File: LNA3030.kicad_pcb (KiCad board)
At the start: 4 copper layers, 11.7 x 8.7 mm, 25 parts, among them P1 SMA-KIT-1.5MF, U1 SWITCH, U2 SWITCH, U3 LNA, U4 SAW

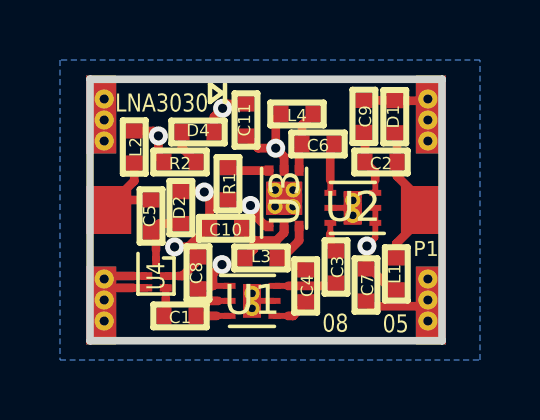
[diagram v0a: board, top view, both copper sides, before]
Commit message: modify for DCC6C SAW filters
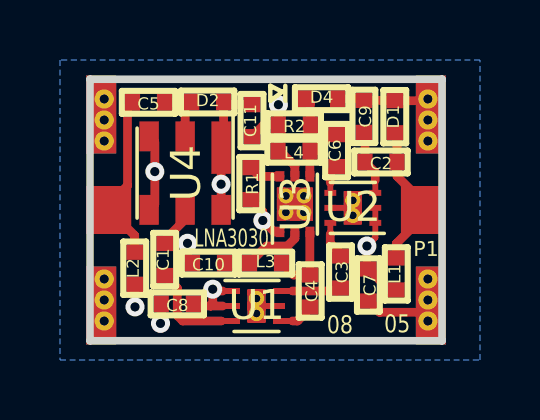
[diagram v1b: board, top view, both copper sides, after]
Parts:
- U4: value SAW -> SAW-DCC6C; footprint gsg-modules:F5Q -> LNA3030:DCC6C
- moved D4 4.27 mm to (132.7, 96.3)
- moved L2 4.04 mm to (126.5, 101.9), turned to 270 degrees
- moved R2 4.01 mm to (131.8, 97.2)
- moved C5 3.79 mm to (127.0, 96.4), turned to 0 degrees
- moved D2 3.63 mm to (128.9, 96.4), turned to 180 degrees
- moved U4 3.56 mm to (128.2, 98.8)
- moved C1 1.95 mm to (127.5, 101.7), turned to 270 degrees
- moved C10 1.29 mm to (128.9, 101.8)
- moved L4 1.24 mm to (131.8, 98.0)
- moved C8 1.24 mm to (127.9, 103.1), turned to 0 degrees
- moved R1 0.76 mm to (130.4, 99.1)
- moved C6 0.66 mm to (133.2, 98.0), turned to 270 degrees
- moved U3 0.41 mm to (131.8, 99.8)
- moved C4 0.23 mm to (132.3, 102.7)
- moved L3 0.23 mm to (130.8, 101.8)
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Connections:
- U4 pad 1: Net-(C5-Pad2) -> GND
- U4 pad 2: GND -> Net-(C5-Pad2)
- U4 pad 4: Net-(C1-Pad1) -> GND
- U4 pad 5: GND -> Net-(C1-Pad1)
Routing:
- net Net-(C1-Pad2): track 1.12 -> 3.48 mm
- net Net-(C5-Pad1): track 3.47 -> 5.69 mm
- net VCC: track 13.5 -> 12.2 mm
- net Net-(C6-Pad2): track 1.68 -> 0.96 mm
- net GND: track 16.0 -> 15.5 mm, vias 3 -> 4

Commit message: correct C7 and C8 part selection
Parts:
- C7, C8: value 47pF -> 100pF
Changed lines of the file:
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@@
       (effects (font (size 0.4064 0.4064) (thickness 0.1016)))
     )
-    (fp_text value 47pF (at 0 0.0508 90) (layer F.SilkS) hide
+    (fp_text value 100pF (at 0 0.0508 90) (layer F.SilkS) hide
       (effects (font (size 0.4064 0.4064) (thickness 0.1016)))
     )
@@
       (effects (font (size 0.4064 0.4064) (thickness 0.1016)))
     )
-    (fp_text value 47pF (at 0 0.0508) (layer F.SilkS) hide
+    (fp_text value 100pF (at 0 0.0508) (layer F.SilkS) hide
       (effects (font (size 0.4064 0.4064) (thickness 0.1016)))
     )
